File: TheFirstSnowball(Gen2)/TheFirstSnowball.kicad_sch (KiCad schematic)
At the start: 65 parts

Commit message: Work for night
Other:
- title: ALP Release Version -> Snowball Project
- moved on the sheet: C1, C10, C2, C3, C4, C5, C6, C7, C8, C9, C?, D1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

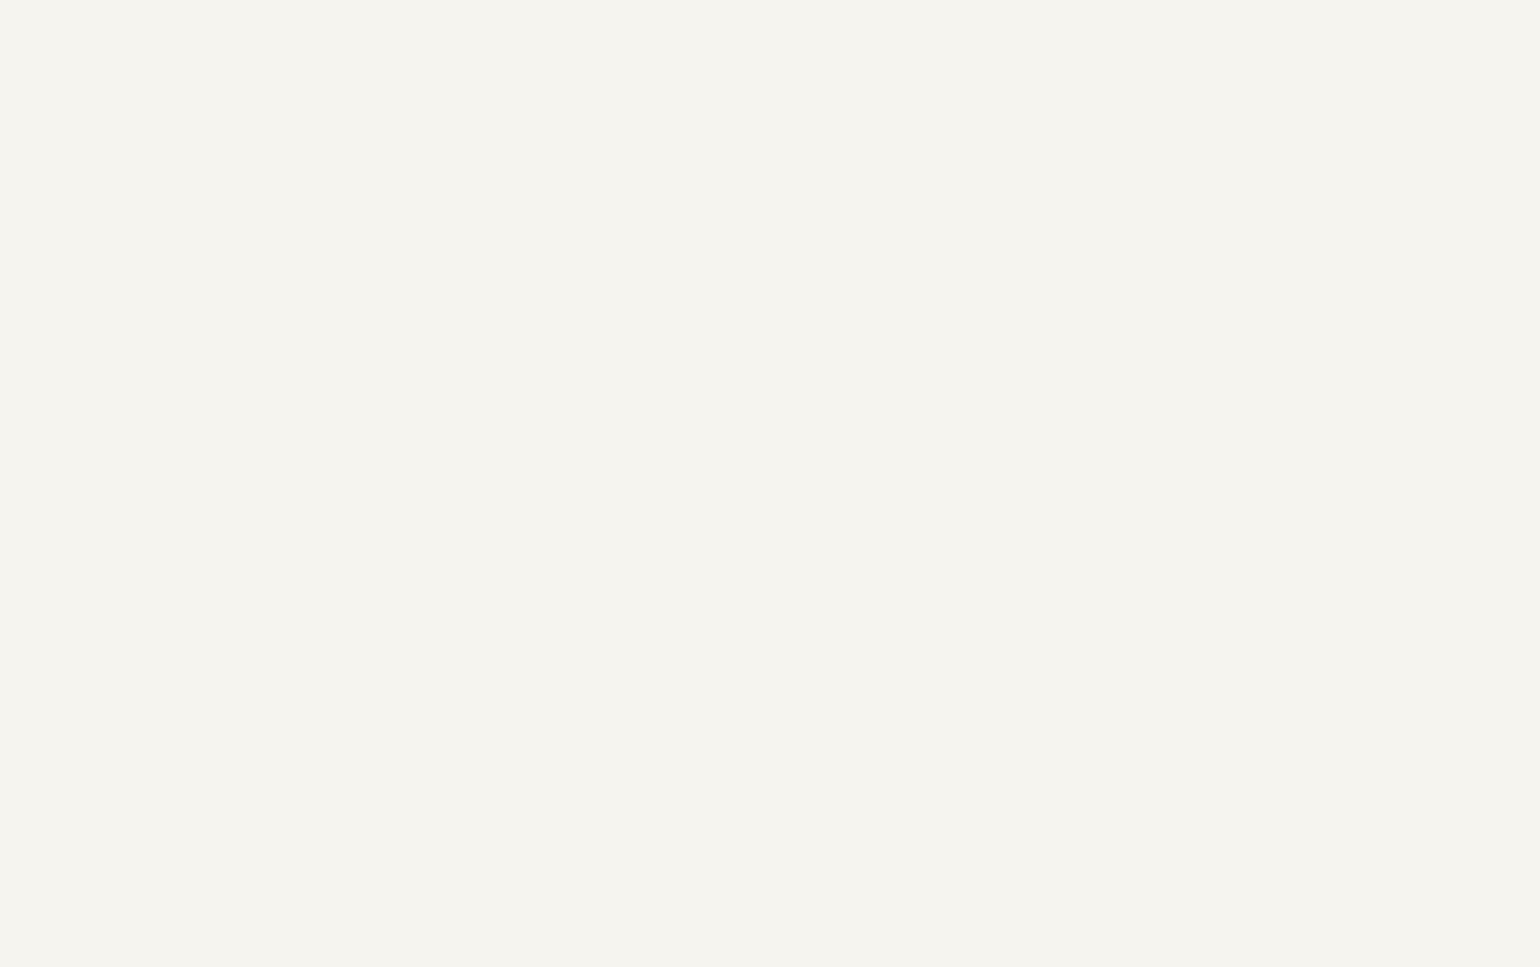
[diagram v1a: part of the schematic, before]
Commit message: Added other input devices based on hardware spec sheet
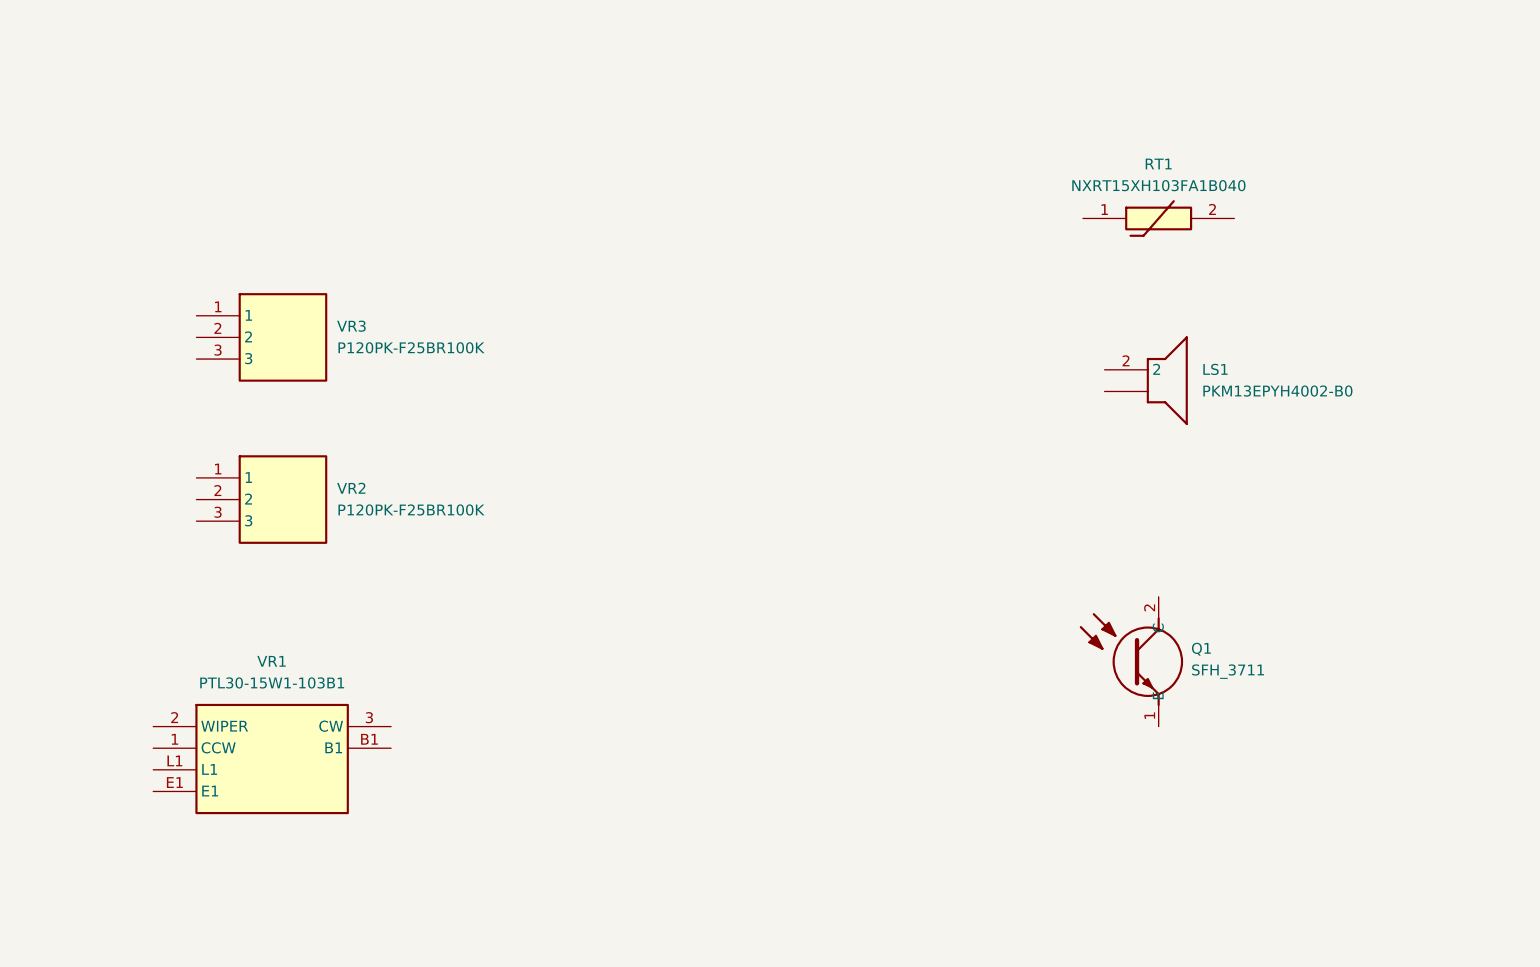
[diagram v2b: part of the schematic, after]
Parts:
- added LS1: PKM13EPYH4002-B0, PKM13EPYH4002-B0, symbol Mouser_LibLoader:PKM13EPYH4002-B0
- added Q1: SFH_3711, SFH3711, symbol Mouser_LibLoader:SFH_3711
- added RT1: NXRT15XH103FA1B040, NXRT15XH103FA1B040, symbol Mouser_LibLoader:NXRT15XH103FA1B040
- added VR1: PTL30-15W1-103B1, PTL3015W1103B1, symbol Mouser_LibLoader:PTL30-15W1-103B1
- added VR2, VR3: P120PK-F25BR100K, P120PKF25BR100K, symbol Mouser_LibLoader:P120PK-F25BR100K

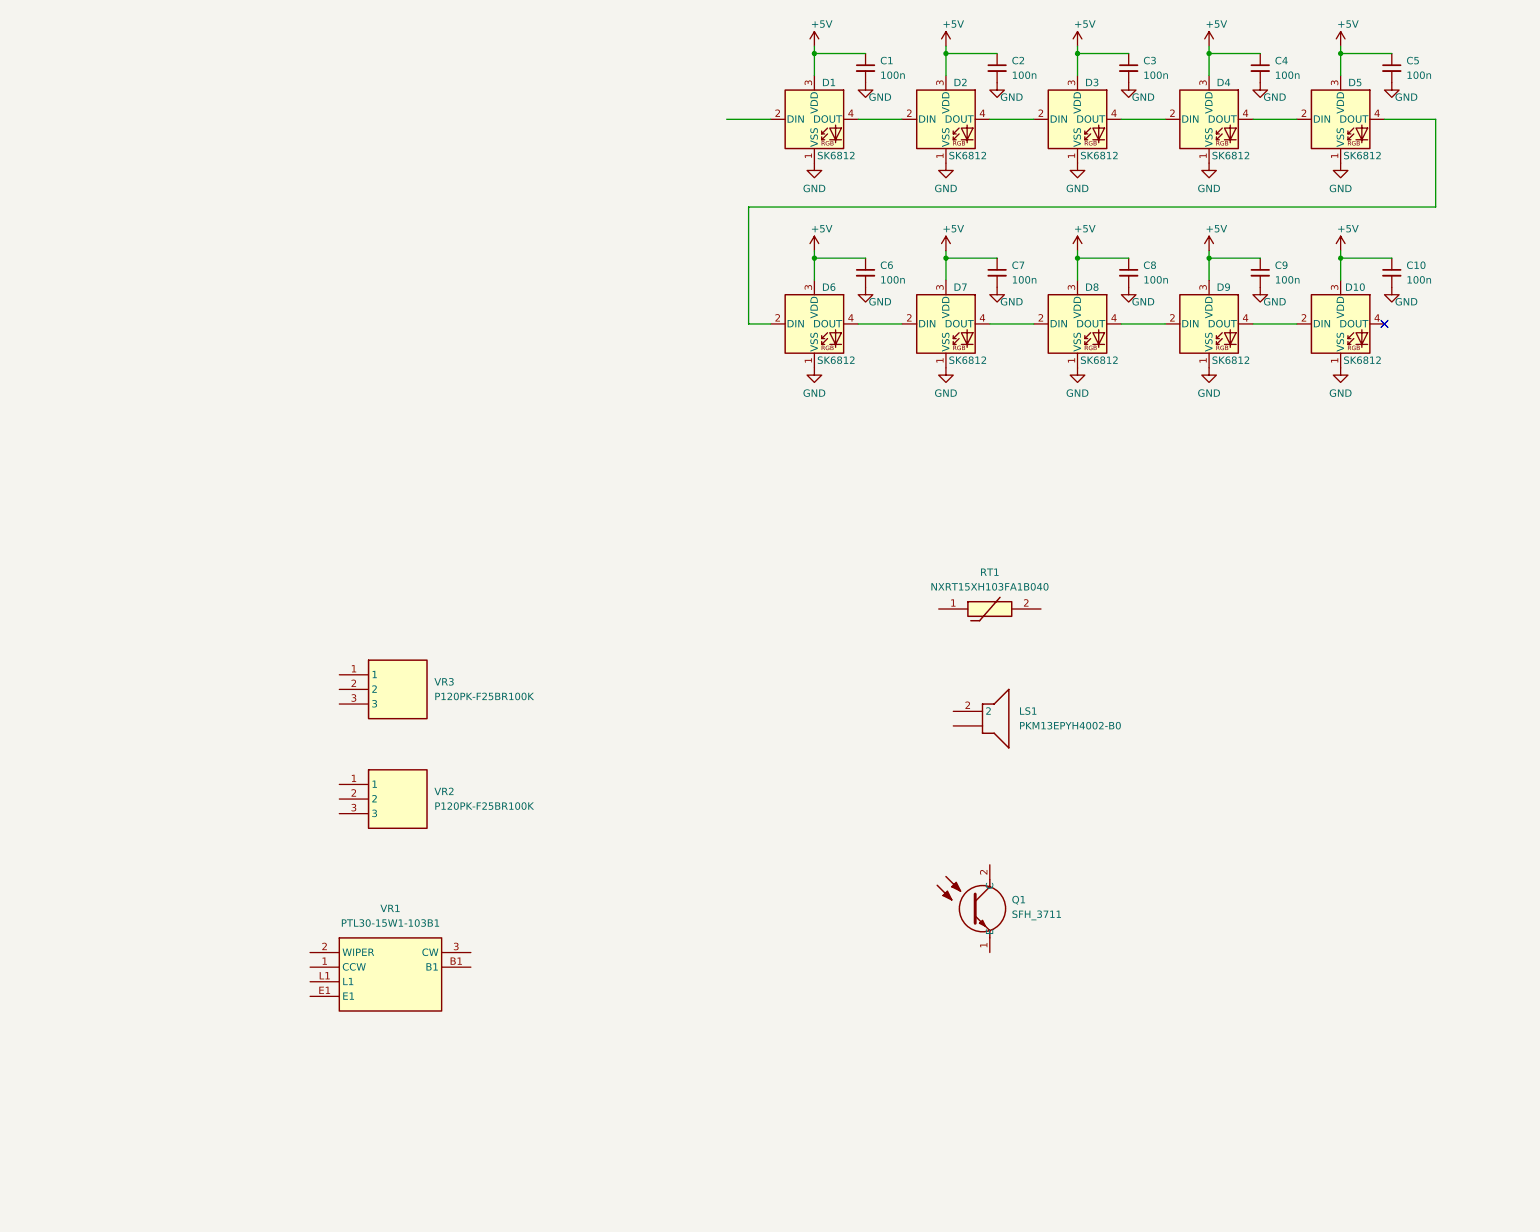
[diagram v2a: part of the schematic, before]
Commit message: Added addressable LEDs
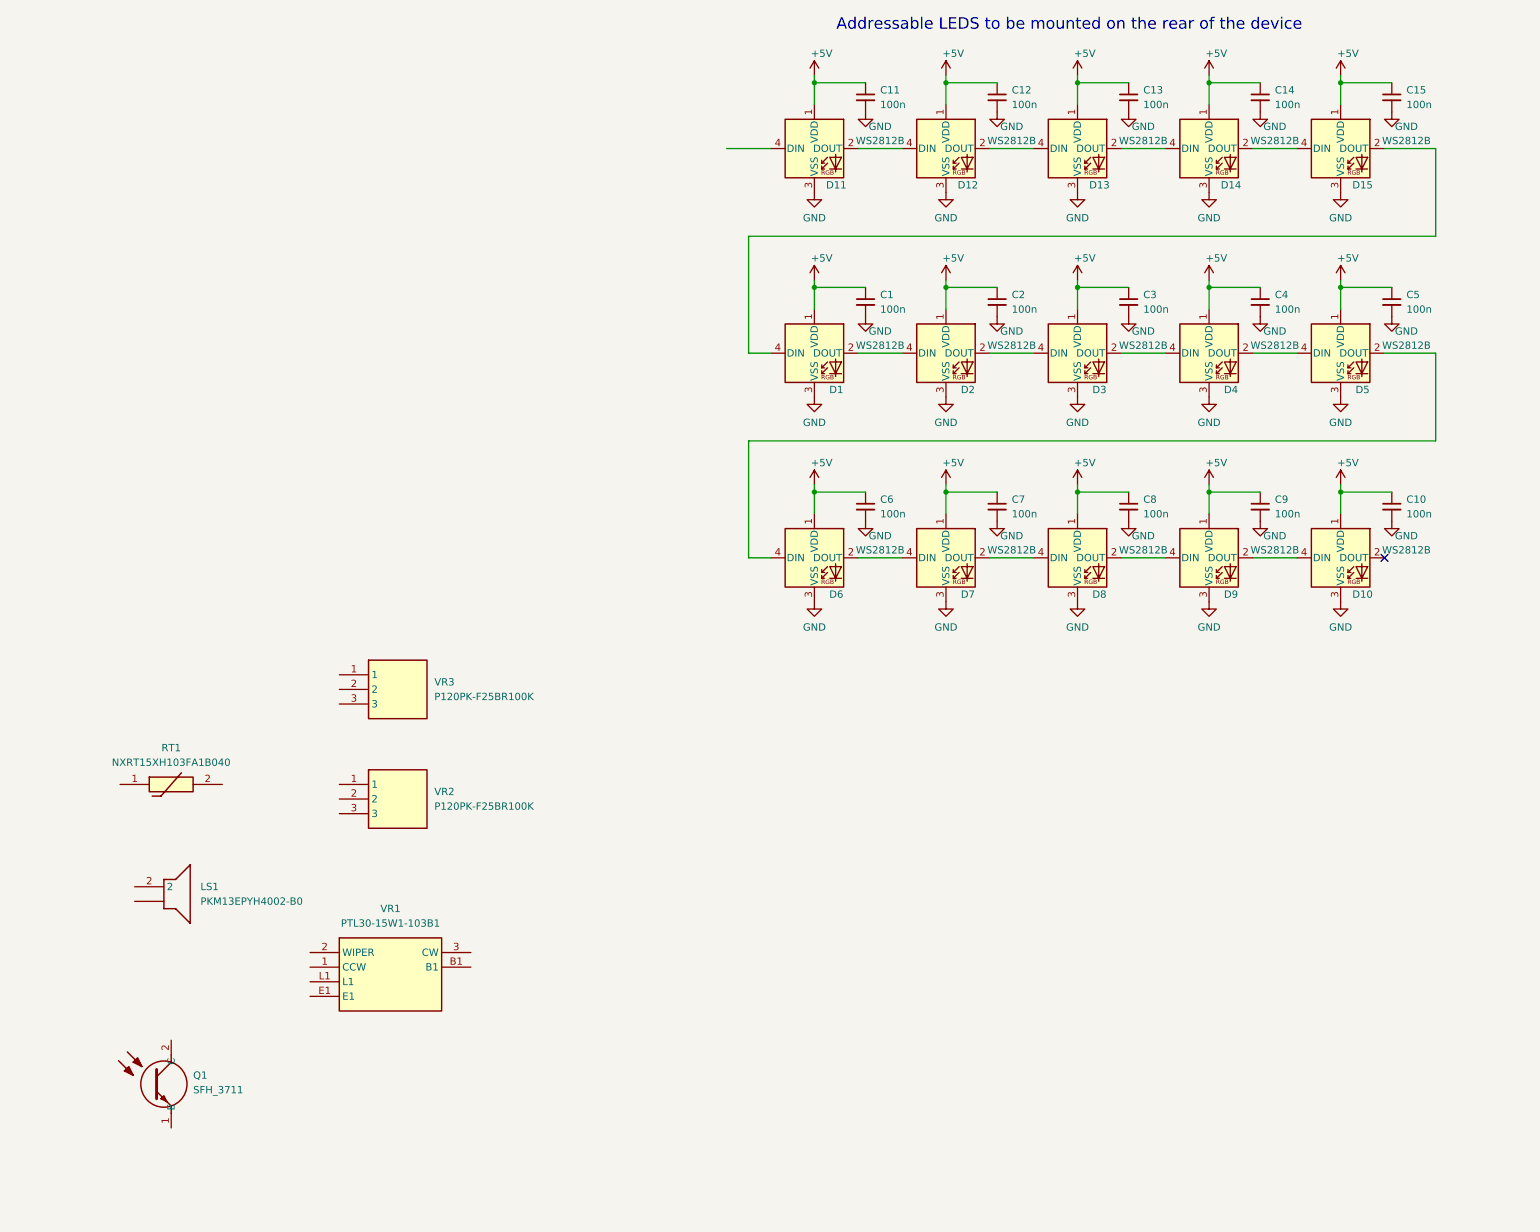
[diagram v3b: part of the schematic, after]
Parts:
- removed D1, D10, D2, D3, D4, D5, D6, D7, D8, D9: SK6812, symbol Rampado_Master:SK6812_Side
- added C11, C12, C13, C14, C15: 100n, symbol Device:C_Small
- added D1, D10, D11, D12, D13, D14, D15, D2, D3, D4, D5, D6, D7, D8, D9: WS2812B, LED_SMD:LED_WS2812B_PLCC4_5.0x5.0mm_P3.2mm, symbol LED:WS2812B
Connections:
- net +5V: now also C11.1, C12.1, C13.1, C14.1, C15.1, D1.1 (VDD), D10.1 (VDD), D11.1 (VDD), D12.1 (VDD), D13.1 (VDD), D14.1 (VDD), D15.1 (VDD), D2.1 (VDD), D3.1 (VDD), D4.1 (VDD), D5.1 (VDD), D6.1 (VDD), D7.1 (VDD), D8.1 (VDD), D9.1 (VDD)
- net GND: now also C11.2, C12.2, C13.2, C14.2, C15.2, D1.3 (VSS), D10.3 (VSS), D11.3 (VSS), D12.3 (VSS), D13.3 (VSS), D14.3 (VSS), D15.3 (VSS), D2.3 (VSS), D3.3 (VSS), D4.3 (VSS), D5.3 (VSS), D6.3 (VSS), D7.3 (VSS), D8.3 (VSS), D9.3 (VSS)
- new net: D10.4 (DIN), D9.2 (DOUT)
- new net: D5.2 (DOUT), D6.4 (DIN)
- new net: D4.2 (DOUT), D5.4 (DIN)
- new net: D3.2 (DOUT), D4.4 (DIN)
- new net: D2.2 (DOUT), D3.4 (DIN)
- new net: D8.2 (DOUT), D9.4 (DIN)
- new net: D7.2 (DOUT), D8.4 (DIN)
- new net: D1.2 (DOUT), D2.4 (DIN)
- new net: D1.4 (DIN), D15.2 (DOUT)
- new net: D13.2 (DOUT), D14.4 (DIN)
- new net: D12.2 (DOUT), D13.4 (DIN)
- new net: D14.2 (DOUT), D15.4 (DIN)
- new net: D6.2 (DOUT), D7.4 (DIN)
- new net: D11.2 (DOUT), D12.4 (DIN)
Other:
- note added: "Addressable LEDS to be mounted on the rear of the device"
- moved on the sheet: C1, C10, C2, C3, C4, C5, C6, C7, C8, C9, LS1, Q1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

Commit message: Added in cool buttons
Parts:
- added S1, S2: D6R00F1LFS, D6R00F1LFS, symbol Mouser_LibLoader:D6R00F1LFS
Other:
- moved on the sheet: D?, LS1, R?, RT1
